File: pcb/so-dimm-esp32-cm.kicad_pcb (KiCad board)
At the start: 4 copper layers, 67.6 x 31.1 mm, 35 parts, among them IC1 PI4IOE5V9535LEX, IC2 PI4IOE5V9535LEX, J1 SODIMM-200, U2 ESP32-S2-SOLO

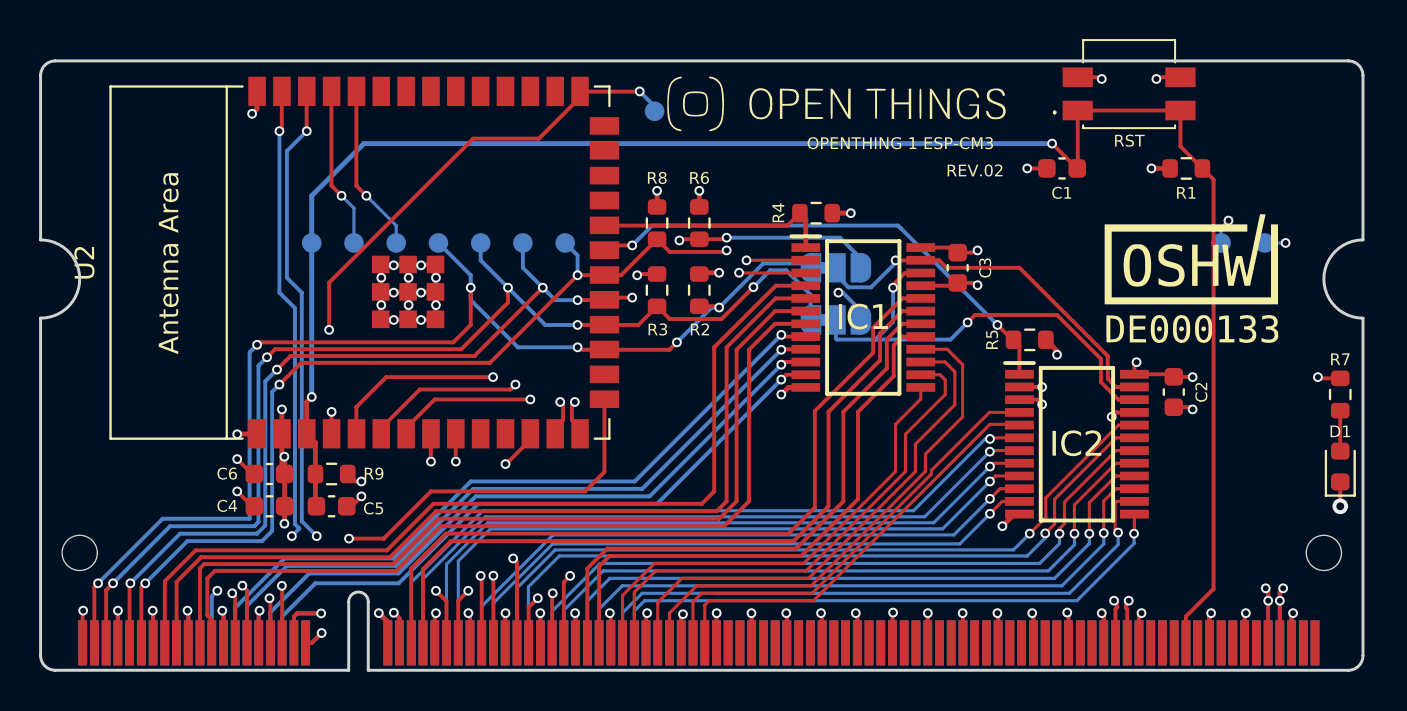
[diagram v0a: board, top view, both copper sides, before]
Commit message: Added Via stitching and ground plane to top and bottom layers
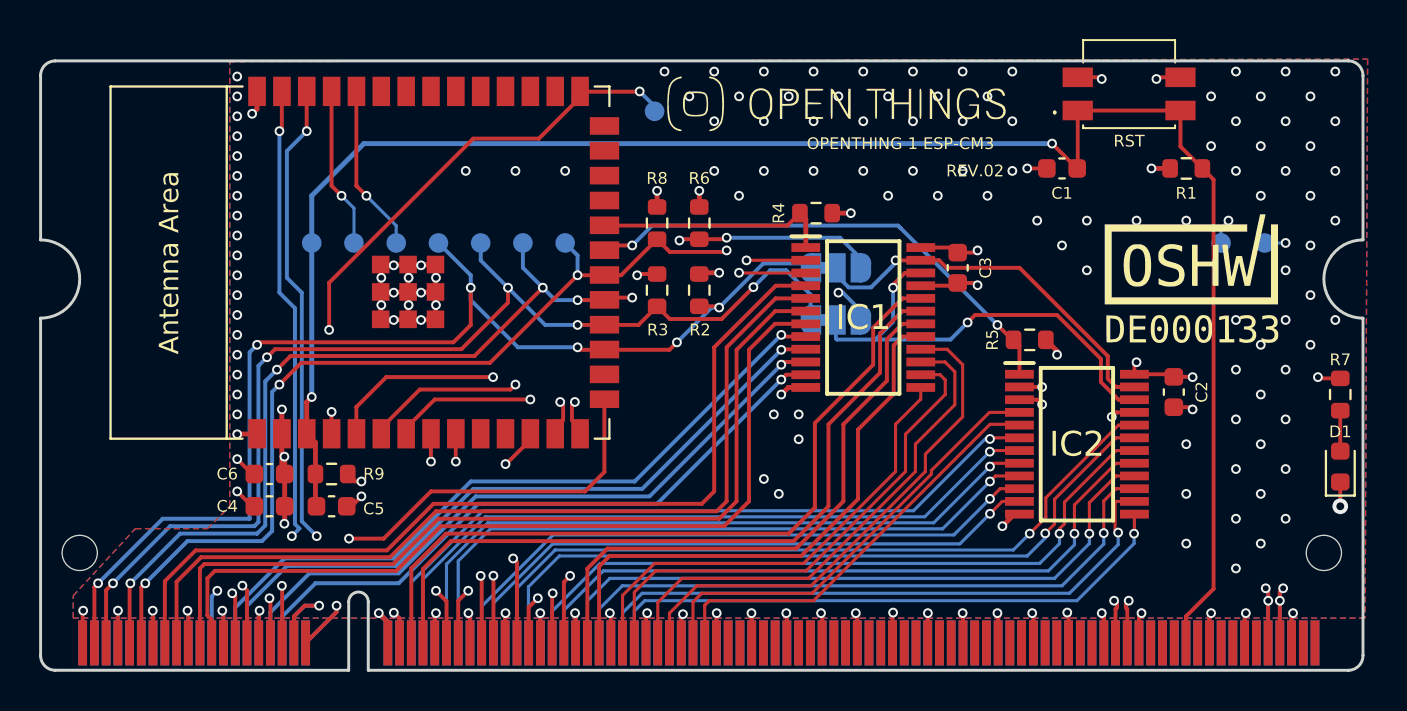
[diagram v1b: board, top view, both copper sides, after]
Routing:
- net +3V3: track 41.4 -> 44.5 mm
- net GND: track 142.0 -> 142.1 mm, vias 62 -> 169
- added copper zone on B.Cu, net GND
- added copper zone on F.Cu, net GND

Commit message: Added CE Sign + Moved footprint a tiny bit + added so-dimm numbering silk + increased revision number
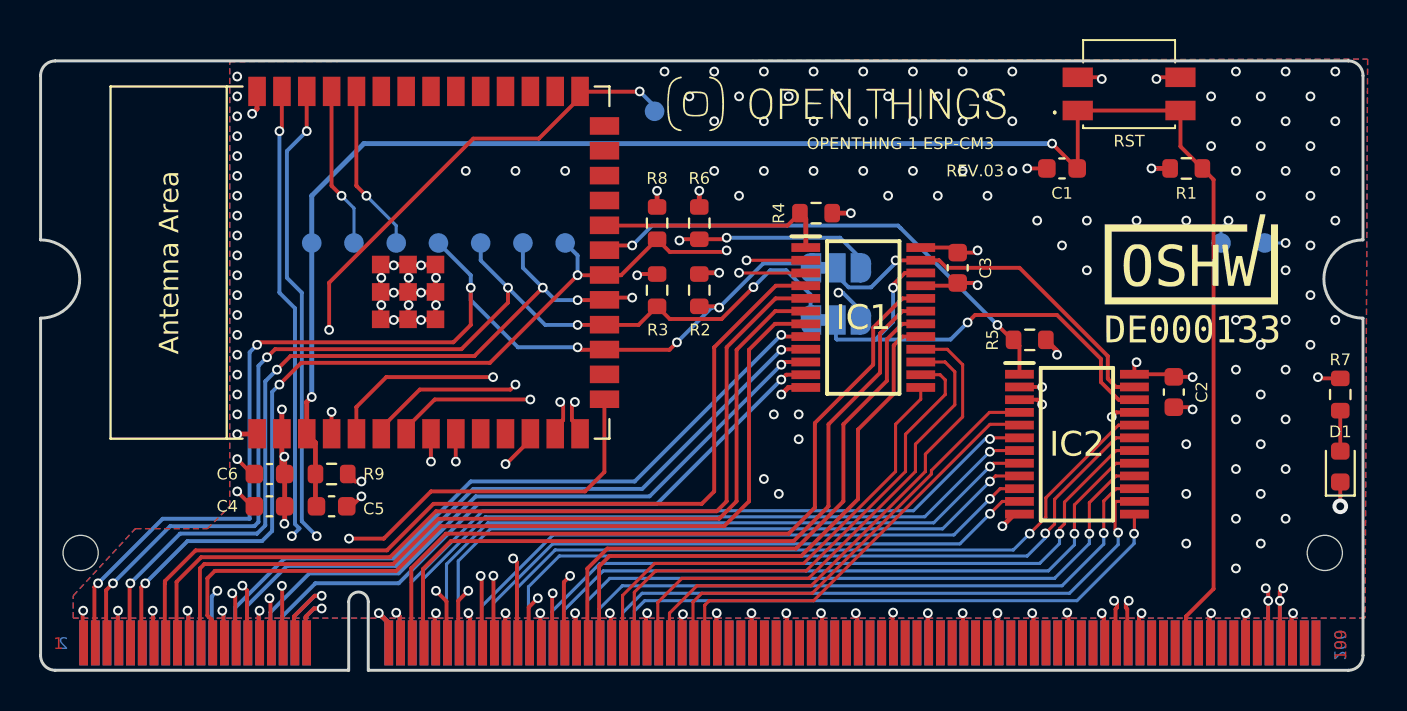
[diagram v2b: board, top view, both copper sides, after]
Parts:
- added REF**: CE-Logo_8.5x6mm_SilkScreen, Symbol:CE-Logo_8.5x6mm_SilkScreen, B.Cu at (176.8, 94.4)
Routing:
- net GND: track 142.1 -> 142.7 mm
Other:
- board text added: "199"
- board text added: "2"
- board text added: "200"
- board text added: "REV.03"
- board text removed: "REV.02"

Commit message: Fix SO-DIMM Pinout differences to DDR2 CM3 + Added ground drill
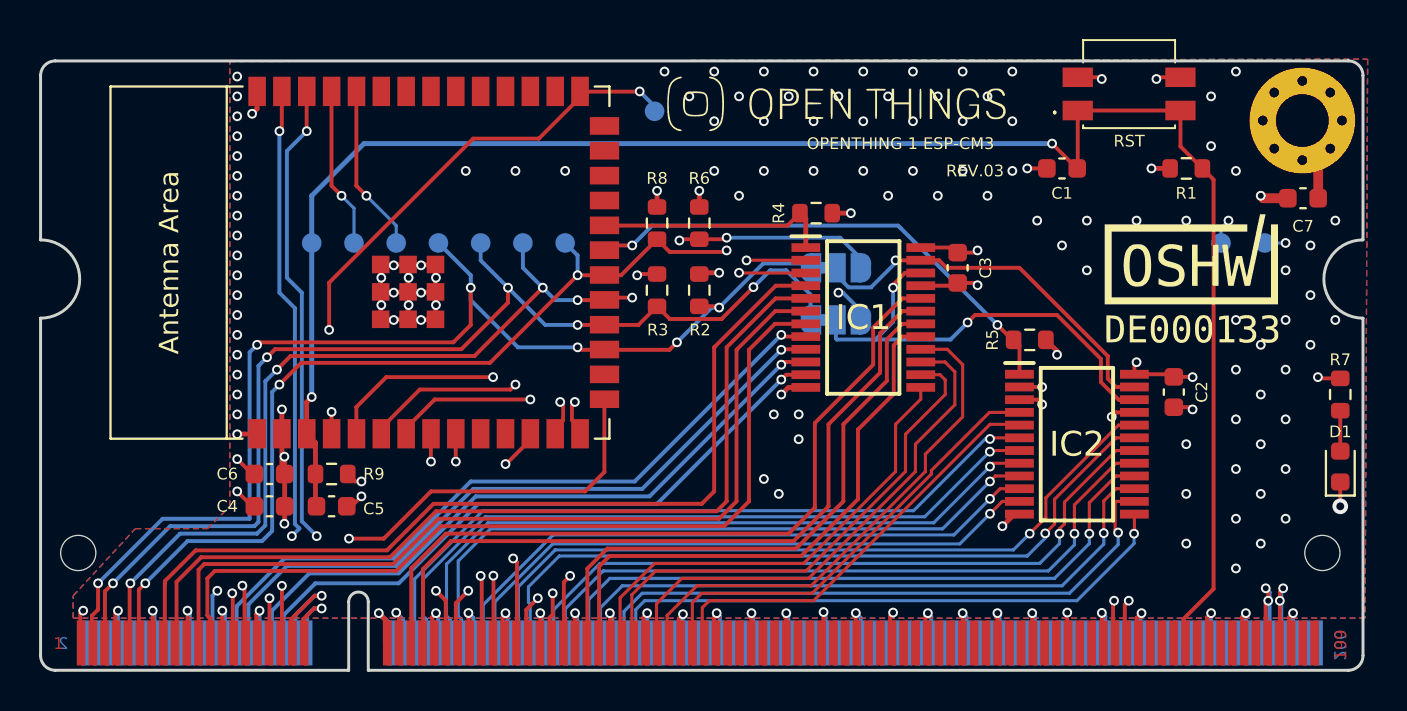
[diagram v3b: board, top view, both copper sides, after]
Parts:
- added C7: DNP, Capacitor_SMD:C_0603_1608Metric, F.Cu at (180.0, 83.9)
- added H1: MountingHole_Pad, MountingHole:MountingHole_2.7mm_Pad_Via, F.Cu at (179.9, 80.0)
- moved J1 0.12 mm to (115.3, 108.1)
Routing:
- net /ESP32-CM/USB_D-: track 38.5 -> 48.5 mm
- net /ESP32-CM/USB_D+: track 36.9 -> 46.8 mm
- net Net-(C7-Pad1): track 0.00 -> 4.31 mm
- net GND: track 142.7 -> 146.2 mm, vias 169 -> 157

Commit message: Add panelisation edges
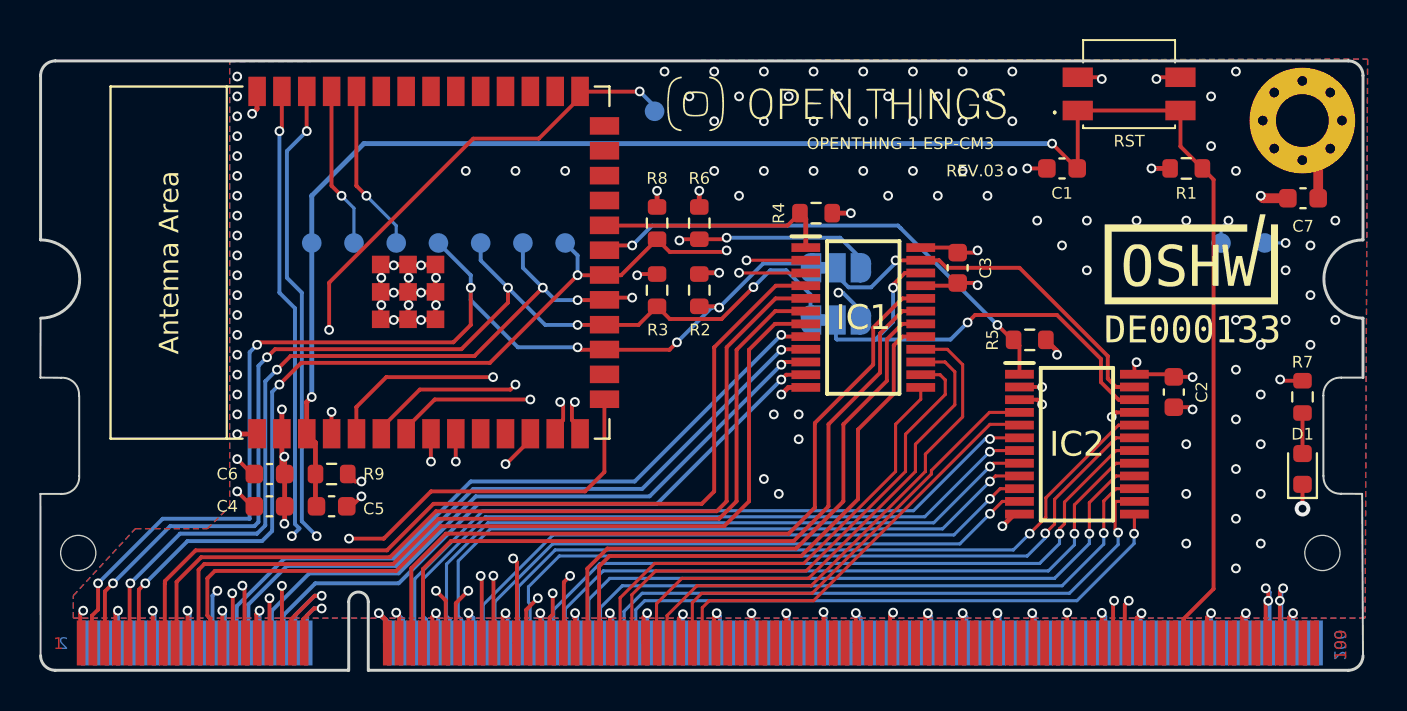
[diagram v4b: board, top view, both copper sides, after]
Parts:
- moved REF** 11.5 mm to (168.7, 86.3)
- moved D1 1.93 mm to (179.9, 97.8)
- moved R7 1.93 mm to (179.9, 94.1)
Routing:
- net GND: vias 157 -> 153
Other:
- outline, holes or cut-outs redrawn

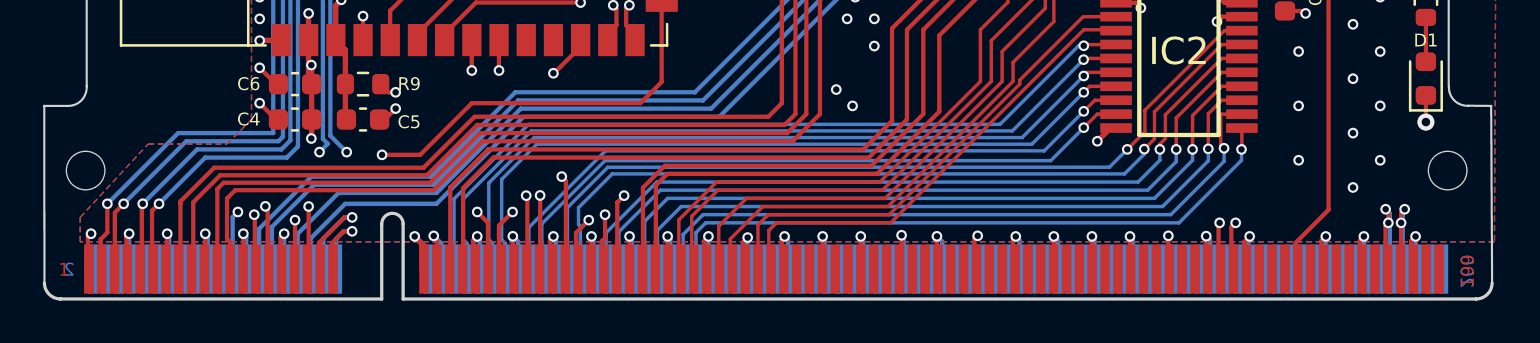
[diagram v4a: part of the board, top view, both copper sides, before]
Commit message: Finally fix SODIMM Pin layout based on datasheet of the 1612618 connector
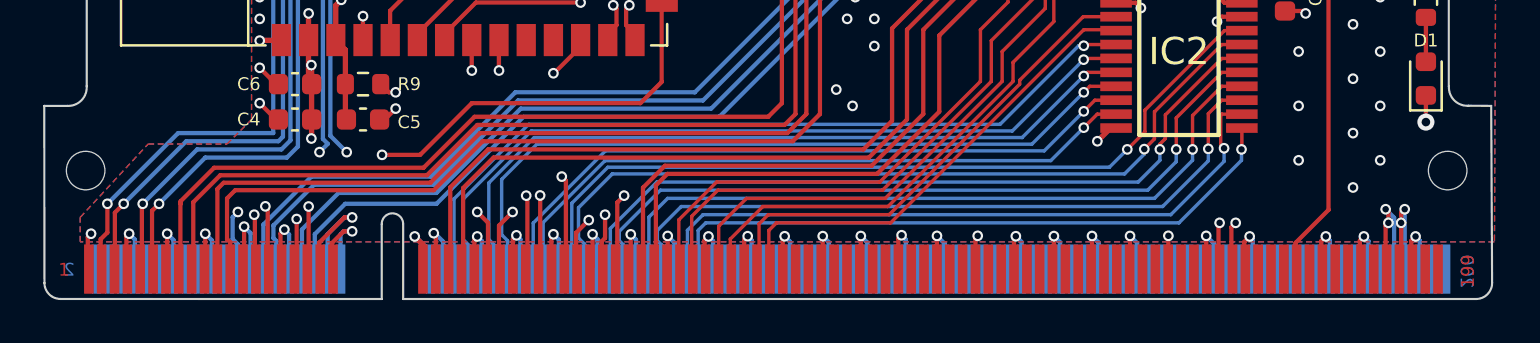
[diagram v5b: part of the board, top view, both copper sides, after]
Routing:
- net GND: track 146.2 -> 150.2 mm

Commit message: Set reset button to be DNP
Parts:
- removed REF**: CE-Logo_8.5x6mm_SilkScreen, Symbol:CE-Logo_8.5x6mm_SilkScreen
- C1: value 0.1uF -> 0.1uF/DNP
- R1: value 10k -> 10k/DNP
